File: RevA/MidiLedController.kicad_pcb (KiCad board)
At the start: 2 copper layers, 99.8 x 100.1 mm, 148 parts, among them J1 Molex 2Way KK254, J12 Barrel_Jack, Q1 MBT3946DW1T1, Q10 MBT3946DW1T1, Q11 MBT3946DW1T1, Q12 MBT3946DW1T1, Q13 MBT3946DW1T1, Q14 MBT3946DW1T1, Q15 MBT3946DW1T1, Q16 MBT3946DW1T1, Q17 MBT3946DW1T1, Q18 MBT3946DW1T1, Q2 MBT3946DW1T1, Q21 DMG2301L, Q3 MBT3946DW1T1, Q4 MBT3946DW1T1, Q5 MBT3946DW1T1, Q6 MBT3946DW1T1, Q7 MBT3946DW1T1, Q8 MBT3946DW1T1, Q9 MBT3946DW1T1, SW1 SW_DIP_x04, SW2 SW_SPST, U1 RAx4_4 1K, U10 RAx4_4 1K, U11 RAx4_4 1K, U12 RAx4_4 1K, U13 RAx4_4 1K, U14 RAx4_4 1K, U15 RAx4_4 1K, U16 RAx4_4 1K, U17 RAx4_4 1K, U18 RAx4_4 1K, U2 RAx4_4 1K, U20 STM32F051K8Tx, U21 6N135S, U22 TPS54202, U23 L7805, U24 MCP1754ST-3302E/CB, U25 NCP51460SN33T1G, U3 RAx4_4 1K, U4 RAx4_4 1K, U5 RAx4_4 1K, U6 RAx4_4 1K, U7 RAx4_4 1K, U8 RAx4_4 1K, U9 RAx4_4 1K

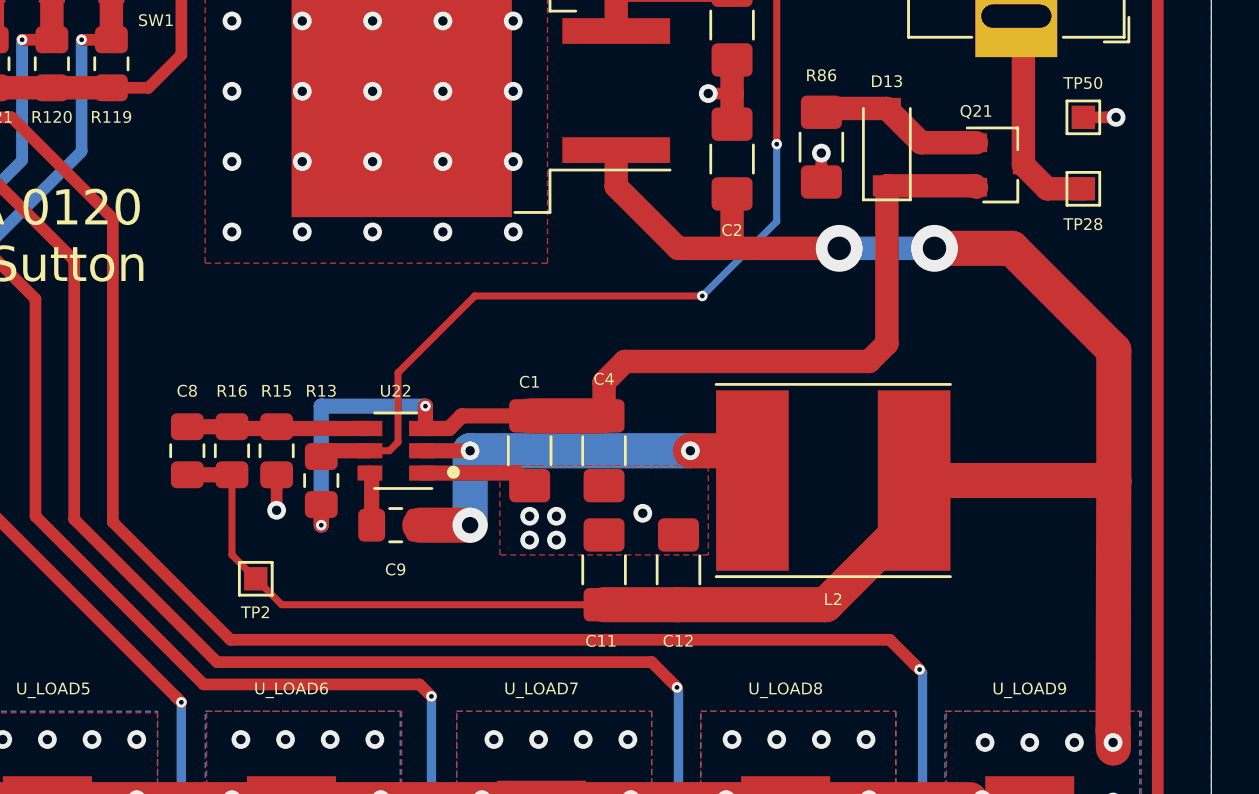
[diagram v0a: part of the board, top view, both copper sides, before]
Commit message: HW: TPS SMPS
- Increased VIN/GNDS trace width and included more ground vias for better thermal management
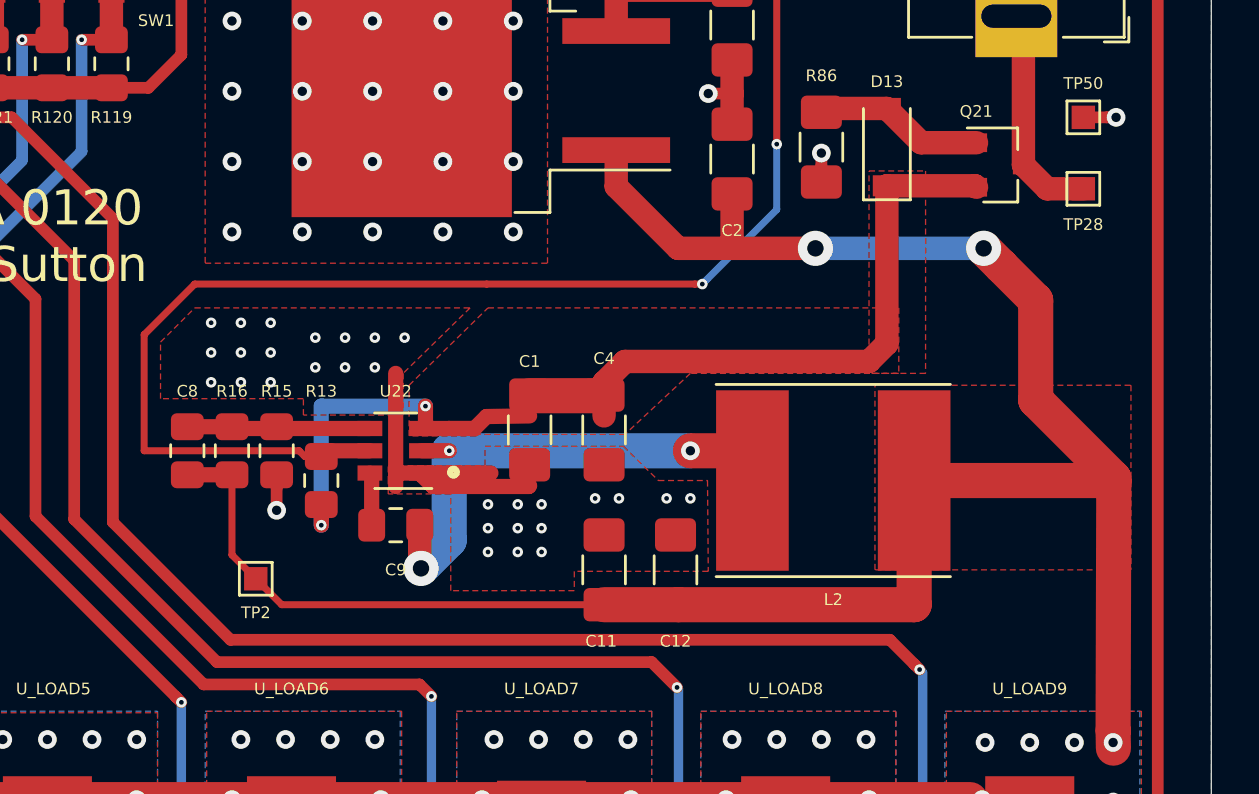
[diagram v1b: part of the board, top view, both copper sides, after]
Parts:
- moved C1 0.89 mm to (164.1, 75.1)
- moved C4 0.89 mm to (167.3, 75.1)
- moved C12 0.13 mm to (170.3, 81.0)
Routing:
- net /PowerSupply/ENSW: track 46.1 -> 64.2 mm
- net GNDS: track 121.9 -> 130.9 mm, vias 96 -> 120
- net Net-(C9-Pad1): track 22.2 -> 24.3 mm
- net VPP: track 186.6 -> 188.1 mm
- added copper zone on F.Cu, net /PowerSupply/VIN_POL

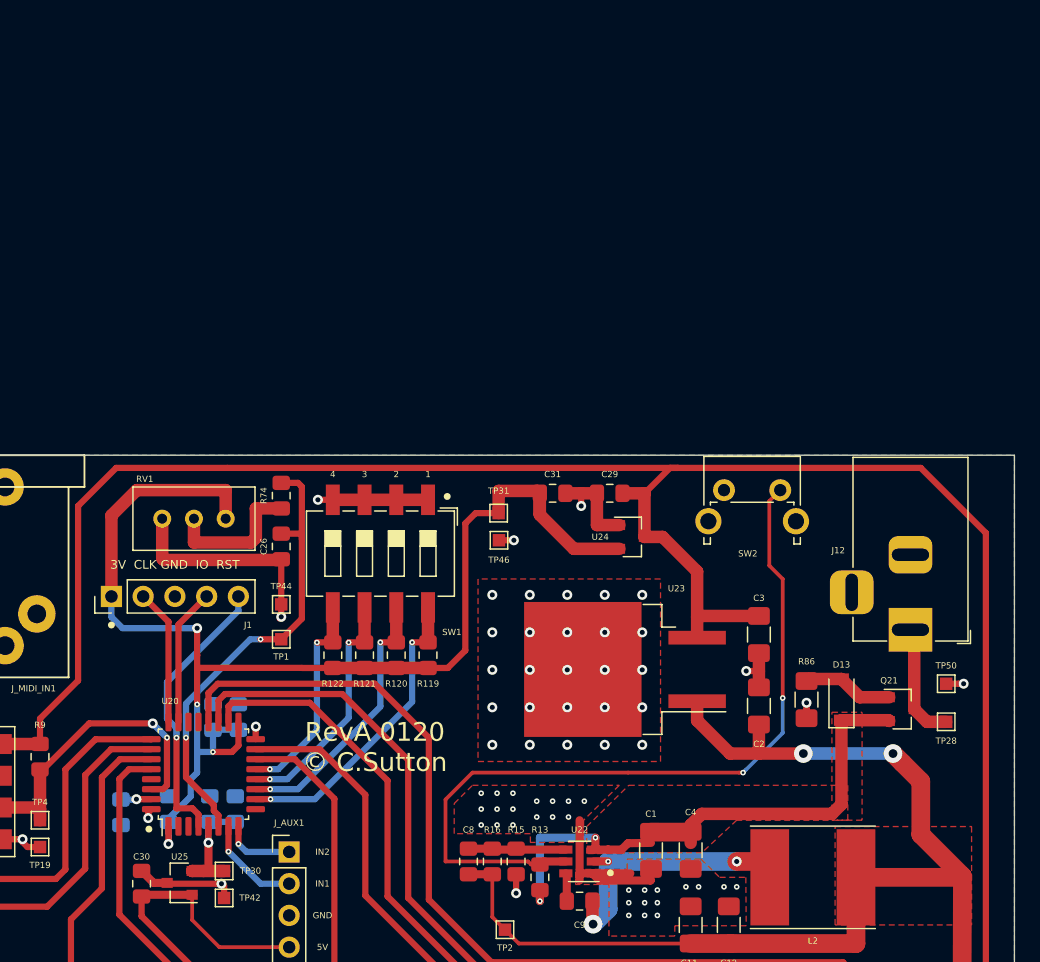
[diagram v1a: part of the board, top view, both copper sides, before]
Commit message: updated HW
changed single gang PTD901 to dual gang concentric PTH901
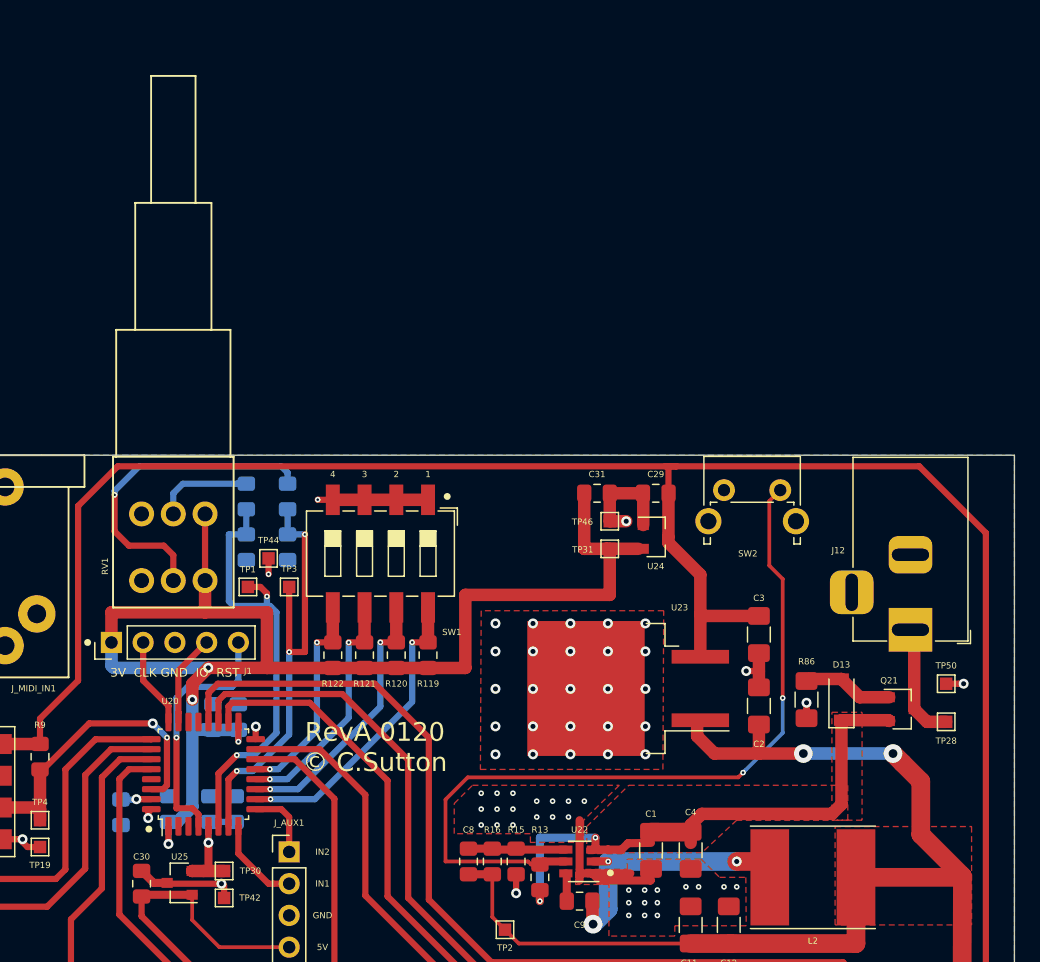
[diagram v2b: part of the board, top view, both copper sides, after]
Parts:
- added C5: 100pF, Capacitor_SMD:C_0805_2012Metric_Pad1.15x1.40mm_HandSolder, B.Cu at (135.0, 50.8)
- added R25: 100R, Resistor_SMD:R_0805_2012Metric_Pad1.15x1.40mm_HandSolder, B.Cu at (135.0, 46.7)
- added TP3: TestPoint, TestPoint:TestPoint_Pad_1.0x1.0mm, F.Cu at (135.1, 54.0)
- C26, R74: moved to B.Cu
- RV1: value B10K PTD901 -> PTH901; footprint Potentiometer_THT:Potentiometer_Bourns_3386C_Horizontal -> PTH901:PTH901
- moved TP31 9.34 mm to (160.8, 50.9)
- moved TP46 8.99 mm to (160.8, 48.7)
- moved TP1 4.97 mm to (131.8, 54.0), turned to 0 degrees
- moved TP44 3.82 mm to (133.5, 51.7)
- moved J1 3.68 mm to (120.9, 58.4)
- moved C29 3.68 mm to (164.5, 46.5)
- moved C31 3.56 mm to (159.8, 46.5)
- moved RV1 2.81 mm to (125.9, 51.2)
- moved C26 2.79 mm to (131.7, 50.8)
- moved R74 2.79 mm to (131.7, 46.7), turned to 270 degrees
- moved U24 1.91 mm to (164.5, 50.0)
- moved U23 1.55 mm to (162.3, 62.1)
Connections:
- J_AUX1 pad 1: /ADC_IN2 -> /ADC_IN3
- J_AUX1 pad 2: /ADC_IN1 -> /ADC_IN2
- U20 pad 9: Net-(U20-Pad9) -> /ADC_IN3
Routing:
- net /ADC_IN1: track 7.94 -> 36.0 mm, vias 1 -> 3
- net Net-(R25-Pad1): track 0.00 -> 26.5 mm, vias 0 -> 1
- net GNDS: track 130.9 -> 114.3 mm, vias 120 -> 119
- net /ADC_IN3: track 0.00 -> 5.74 mm
- net /SWCLK: track 10.9 -> 7.21 mm
- net /SWDIO: track 11.0 -> 7.31 mm
- net Net-(R74-Pad1): track 11.4 -> 7.81 mm
- net +3V3: track 107.8 -> 110.7 mm
- net +5V: track 591.2 -> 588.3 mm
- net /NRST: track 22.6 -> 20.3 mm
- net /ADC_IN0: track 37.4 -> 35.5 mm
- net /ADC_IN2: track 5.73 -> 7.24 mm, vias 1 -> 0
- net VPP: track 188.1 -> 187.3 mm
